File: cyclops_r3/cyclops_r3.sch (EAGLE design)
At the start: 105 parts, among them Q1 BC817, Q2 IRF510, U1 MCP4921, U2 MCP4022-50k, U3 317-N, U4 TLV3701, U5 337-N, U6 ADR03, U7 OP1177, U8 LTC2052HV, U9 ZXTD45

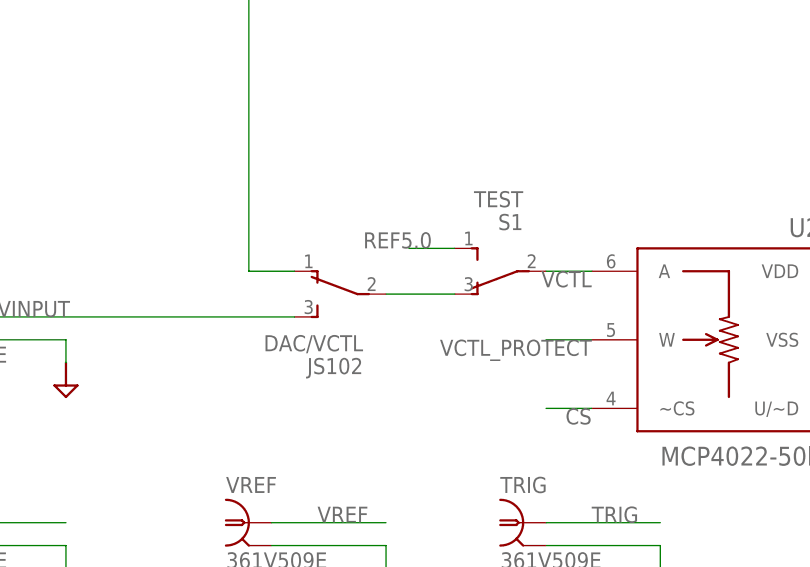
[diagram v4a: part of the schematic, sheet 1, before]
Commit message: The hole size for the solder lugs on the DAC/VCTL switch were too small. This has been fixed.
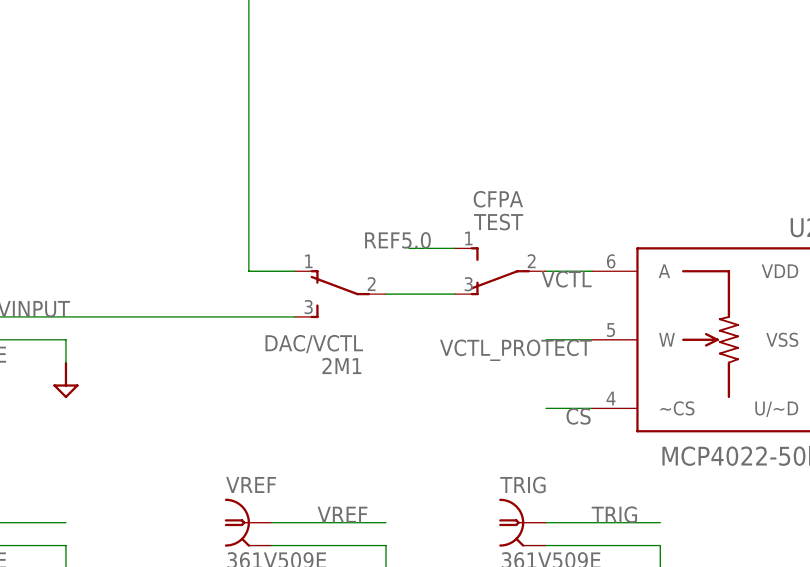
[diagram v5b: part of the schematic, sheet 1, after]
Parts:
- DAC/VCTL: value JS102 -> 2M1
- TEST: value TEST -> CFPA
- renumbered S1 to TEST
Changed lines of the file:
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@@
 <part name="C17" library="cyclops" deviceset="C" device="_0805" value="1uF"/>
 <part name="C11" library="cyclops" deviceset="C-POL" device="_0807" value="100uF"/>
-<part name="S1" library="cyclops" deviceset="SPDT" device="_CFPA" value="TEST"/>
+<part name="TEST" library="cyclops" deviceset="SPDT" device="_CFPA" value="CFPA"/>
 <part name="U9" library="cyclops" deviceset="ZXTD4591E6" device="" value="ZXTD45"/>
 <part name="Q2" library="cyclops" deviceset="N-MOSFET" device="TO-262" value="IRF510"/>
@@
 <part name="PWR_IN" library="cyclops" deviceset="PINH1X3" device="_MINI-JR" value="PINH1X3_MINI-JR"/>
 <part name="GAIN" library="cyclops" deviceset="POT_US" device="_3310" value="1k"/>
-<part name="DAC/VCTL" library="cyclops" deviceset="SPDT" device="_MTS-M6" value="JS102"/>
+<part name="DAC/VCTL" library="cyclops" deviceset="SPDT" device="_MTS-M6" value="2M1"/>
 <part name="L6" library="cyclops" deviceset="L" device="_0603" value="MPZ1608"/>
 <part name="L5" library="cyclops" deviceset="L" device="_0603" value="MPZ1608"/>
@@
 <instance part="FRAME1" gate="G$1" x="-12.7" y="-68.58"/>
 <instance part="FRAME1" gate="G$2" x="160.02" y="-68.58"/>
-<instance part="S1" gate="G$1" x="210.82" y="20.32" rot="R180"/>
+<instance part="TEST" gate="G$1" x="210.82" y="20.32" rot="R180"/>
 <instance part="VAUX_OUT" gate="G$1" x="109.22" y="15.24"/>
 <instance part="CS1" gate="1" x="109.22" y="121.92" smashed="yes">
@@
 <segment>
 <wire x1="195.58" y1="17.78" x2="203.2" y2="17.78" width="0.1524" layer="91"/>
-<pinref part="S1" gate="G$1" pin="1"/>
+<pinref part="TEST" gate="G$1" pin="1"/>
 <pinref part="DAC/VCTL" gate="G$1" pin="2"/>
 </segment>
@@
 <net name="VCTL" class="0">
 <segment>
-<pinref part="S1" gate="G$1" pin="2"/>
+<pinref part="TEST" gate="G$1" pin="2"/>
 <wire x1="213.36" y1="20.32" x2="218.44" y2="20.32" width="0.1524" layer="91"/>
 <pinref part="U2" gate="G$1" pin="A"/>
@@
 <net name="REF5.0" class="0">
 <segment>
-<pinref part="S1" gate="G$1" pin="3"/>
+<pinref part="TEST" gate="G$1" pin="3"/>
 <wire x1="203.2" y1="22.86" x2="198.12" y2="22.86" width="0.1524" layer="91"/>
 <label x="193.04" y="22.86" size="1.778" layer="95"/>

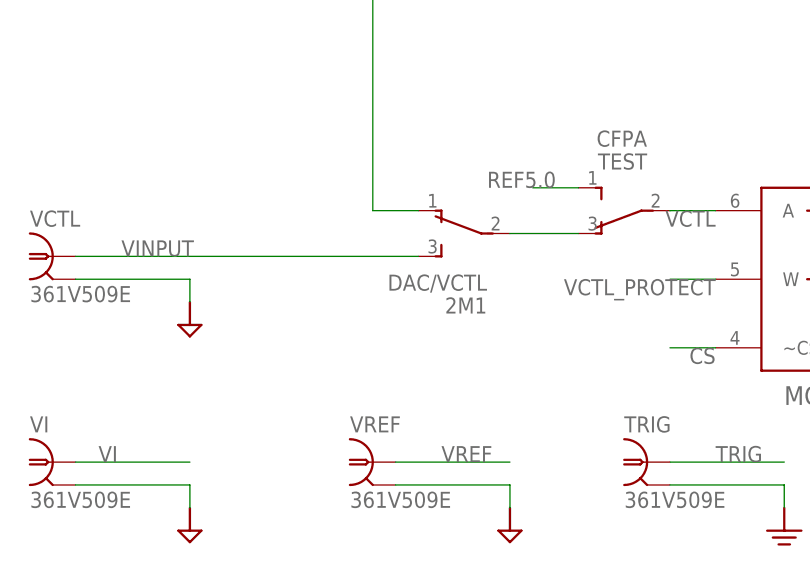
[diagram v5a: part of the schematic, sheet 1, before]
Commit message: Assembed r3.3 and started a TODO list. Started driver code.
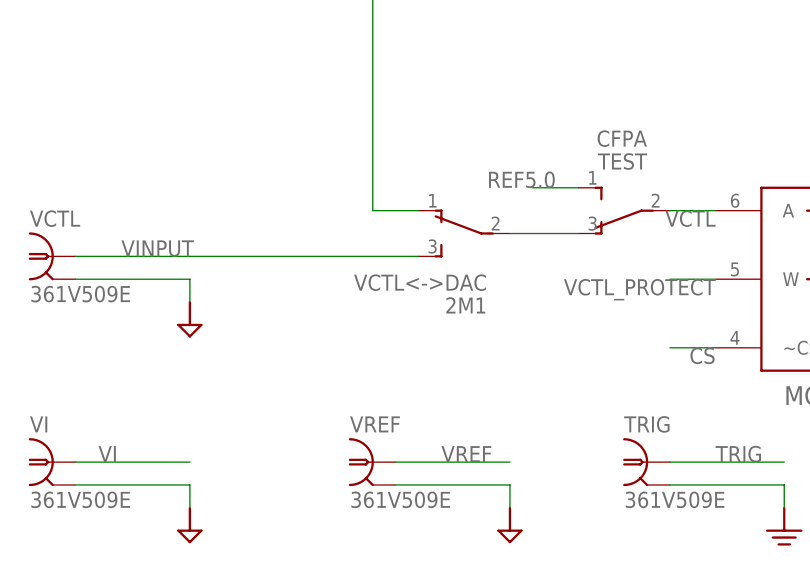
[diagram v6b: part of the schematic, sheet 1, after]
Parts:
- renumbered CURR/AUX to AUX<->CURR, DAC/VCTL to VCTL<->DAC
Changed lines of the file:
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@@
 <?xml version="1.0" encoding="utf-8"?>
 <!DOCTYPE eagle SYSTEM "eagle.dtd">
-<eagle version="6.5.0">
+<eagle version="6.6.0">
 <drawing>
 <settings>
@@
 <part name="D3" library="cyclops" deviceset="S-DIODE" device="SOD-123" value="DS11015"/>
 <part name="D2" library="cyclops" deviceset="S-DIODE" device="SOD-123" value="DS11015"/>
-<part name="CURR/AUX" library="cyclops" deviceset="SPDT" device="_JS" value="JS102"/>
+<part name="AUX&lt;-&gt;CURR" library="cyclops" deviceset="SPDT" device="_JS" value="JS102"/>
 <part name="FRAME1" library="cyclops" deviceset="FRAME_A_L" device=""/>
 <part name="FRAME2" library="cyclops" deviceset="FRAME_A_L" device=""/>
@@
 <part name="PWR_IN" library="cyclops" deviceset="PINH1X3" device="_MINI-JR" value="PINH1X3_MINI-JR"/>
 <part name="GAIN" library="cyclops" deviceset="POT_US" device="_3310" value="1k"/>
-<part name="DAC/VCTL" library="cyclops" deviceset="SPDT" device="_MTS-M6" value="2M1"/>
+<part name="VCTL&lt;-&gt;DAC" library="cyclops" deviceset="SPDT" device="_MTS-M6" value="2M1"/>
 <part name="L6" library="cyclops" deviceset="L" device="_0603" value="MPZ1608"/>
 <part name="L5" library="cyclops" deviceset="L" device="_0603" value="MPZ1608"/>
@@
 <instance part="PWR_DIST" gate="G$1" x="33.02" y="-20.32"/>
 <instance part="PWR_IN" gate="G$1" x="25.4" y="5.08"/>
-<instance part="DAC/VCTL" gate="G$1" x="193.04" y="17.78" rot="MR0"/>
+<instance part="VCTL&lt;-&gt;DAC" gate="G$1" x="193.04" y="17.78" rot="MR0"/>
 <instance part="L6" gate="L" x="53.34" y="38.1" smashed="yes">
 <attribute name="NAME" x="52.07" y="30.48" size="1.778" layer="95" rot="R90"/>
@@
 <wire x1="172.72" y1="78.74" x2="172.72" y2="81.28" width="0.1524" layer="91"/>
 <junction x="172.72" y="81.28"/>
-<pinref part="DAC/VCTL" gate="G$1" pin="1"/>
+<pinref part="VCTL&lt;-&gt;DAC" gate="G$1" pin="1"/>
 <wire x1="180.34" y1="20.32" x2="185.42" y2="20.32" width="0.1524" layer="91"/>
 <wire x1="180.34" y1="81.28" x2="180.34" y2="20.32" width="0.1524" layer="91"/>
@@
 <pinref part="VCTL" gate="G$1" pin="1"/>
 <label x="152.4" y="15.24" size="1.778" layer="95"/>
-<pinref part="DAC/VCTL" gate="G$1" pin="3"/>
+<pinref part="VCTL&lt;-&gt;DAC" gate="G$1" pin="3"/>
 <wire x1="185.42" y1="15.24" x2="147.32" y2="15.24" width="0.1524" layer="91"/>
 </segment>
@@
 <wire x1="195.58" y1="17.78" x2="203.2" y2="17.78" width="0.1524" layer="91"/>
 <pinref part="TEST" gate="G$1" pin="1"/>
-<pinref part="DAC/VCTL" gate="G$1" pin="2"/>
+<pinref part="VCTL&lt;-&gt;DAC" gate="G$1" pin="2"/>
 </segment>
 </net>
@@
 <instance part="D3" gate="G$1" x="-10.16" y="73.66" rot="R90"/>
 <instance part="D2" gate="G$1" x="-10.16" y="99.06" rot="R90"/>
-<instance part="CURR/AUX" gate="G$1" x="7.62" y="48.26" rot="MR270"/>
+<instance part="AUX&lt;-&gt;CURR" gate="G$1" x="7.62" y="48.26" rot="MR270"/>
 <instance part="FRAME4" gate="G$1" x="-91.44" y="-58.42"/>
 <instance part="U9" gate="G$1" x="83.82" y="83.82"/>
@@
 <wire x1="10.16" y1="20.32" x2="68.58" y2="20.32" width="0.1524" layer="91"/>
 <junction x="68.58" y="20.32"/>
-<pinref part="CURR/AUX" gate="G$1" pin="3"/>
+<pinref part="AUX&lt;-&gt;CURR" gate="G$1" pin="3"/>
 <wire x1="10.16" y1="40.64" x2="10.16" y2="20.32" width="0.1524" layer="91"/>
 </segment>
@@
 <wire x1="7.62" y1="50.8" x2="7.62" y2="81.28" width="0.1524" layer="91"/>
 <pinref part="U8" gate="B" pin="-IN"/>
-<pinref part="CURR/AUX" gate="G$1" pin="2"/>
+<pinref part="AUX&lt;-&gt;CURR" gate="G$1" pin="2"/>
 </segment>
 </net>
@@
 <wire x1="-35.56" y1="35.56" x2="-35.56" y2="38.1" width="0.1524" layer="91"/>
 <junction x="-35.56" y="35.56"/>
-<pinref part="CURR/AUX" gate="G$1" pin="1"/>
+<pinref part="AUX&lt;-&gt;CURR" gate="G$1" pin="1"/>
 <wire x1="5.08" y1="35.56" x2="5.08" y2="40.64" width="0.1524" layer="91"/>
 <junction x="5.08" y="35.56"/>

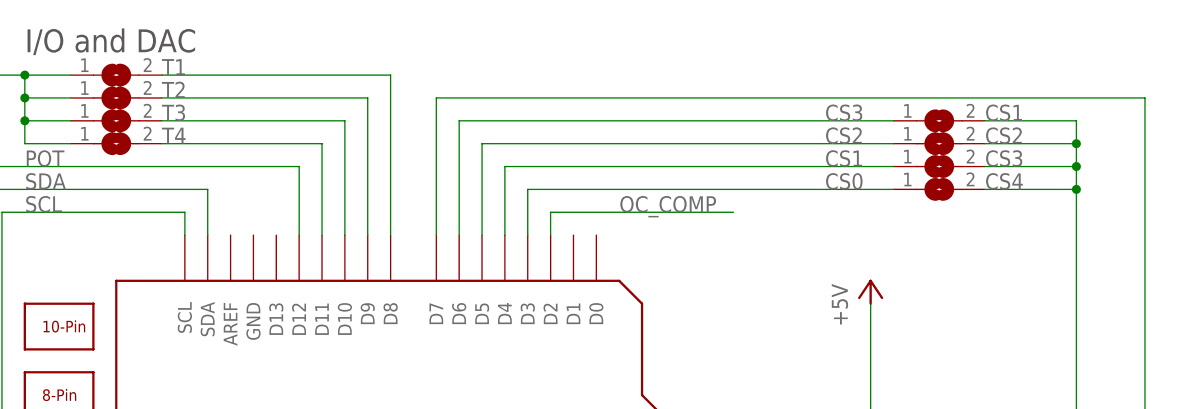
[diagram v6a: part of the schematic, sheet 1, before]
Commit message: Asthetic fixes to board. Driver has limited functionality and is pretty inefficient, but the base stuff is there.
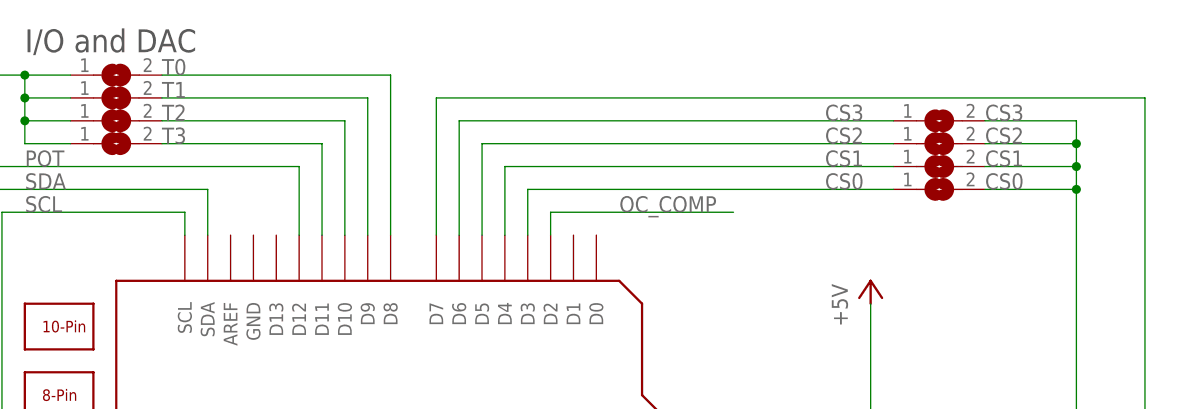
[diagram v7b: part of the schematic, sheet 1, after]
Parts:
- removed T4: (no value), cyclops:SJ
- added T0: (no value), cyclops:SJ
- renumbered CS4 to CS0
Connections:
- net CS1: now also CS1.1; no longer CS3.1
- net CS3: now also CS3.1; no longer CS1.1
- net T0: now also T0.2; no longer T1.2
- net T1: now also T1.2; no longer T2.2
- net T2: now also T2.2; no longer T3.2
- net T3: now also T3.2; no longer T4.2
- net TRIG: now also T0.1; no longer T4.1
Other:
- moved on the sheet: CS1, CS3, T1, T2, T3
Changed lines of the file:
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@@
 <part name="C24" library="cyclops" deviceset="C" device="_0805" value="1uF"/>
 <part name="C22" library="cyclops" deviceset="C" device="_0603" value=".1uF"/>
+<part name="CS3" library="cyclops" deviceset="SJ" device=""/>
+<part name="CS2" library="cyclops" deviceset="SJ" device=""/>
 <part name="CS1" library="cyclops" deviceset="SJ" device=""/>
-<part name="CS2" library="cyclops" deviceset="SJ" device=""/>
-<part name="CS3" library="cyclops" deviceset="SJ" device=""/>
-<part name="CS4" library="cyclops" deviceset="SJ" device=""/>
+<part name="CS0" library="cyclops" deviceset="SJ" device=""/>
 <part name="Q1" library="cyclops" deviceset="BC817*" device="SMD" technology="-16" value="BC817"/>
 <part name="R8" library="cyclops" deviceset="R" device="_0603" value="10k"/>
@@
 <part name="P+5" library="cyclops" deviceset="+5V" device="" value="+12V"/>
 <part name="R20" library="cyclops" deviceset="R" device="_0603" value="220k"/>
+<part name="T0" library="cyclops" deviceset="SJ" device=""/>
 <part name="T1" library="cyclops" deviceset="SJ" device=""/>
 <part name="T2" library="cyclops" deviceset="SJ" device=""/>
 <part name="T3" library="cyclops" deviceset="SJ" device=""/>
-<part name="T4" library="cyclops" deviceset="SJ" device=""/>
 <part name="TRIG" library="cyclops" deviceset="BNC" device="_V-BITE" value="361V509E"/>
 <part name="U$47" library="cyclops" deviceset="GND1" device=""/>
@@
 <instance part="TEST" gate="G$1" x="210.82" y="20.32" rot="R180"/>
 <instance part="VAUX_OUT" gate="G$1" x="109.22" y="15.24"/>
-<instance part="CS1" gate="1" x="109.22" y="121.92" smashed="yes">
+<instance part="CS3" gate="1" x="109.22" y="121.92" smashed="yes">
 <attribute name="NAME" x="114.3" y="121.92" size="1.778" layer="95"/>
 <attribute name="VALUE" x="106.68" y="118.11" size="1.778" layer="96"/>
@@
 <attribute name="VALUE" x="106.68" y="115.57" size="1.778" layer="96"/>
 </instance>
-<instance part="CS3" gate="1" x="109.22" y="116.84" smashed="yes">
+<instance part="CS1" gate="1" x="109.22" y="116.84" smashed="yes">
 <attribute name="NAME" x="114.3" y="116.84" size="1.778" layer="95"/>
 <attribute name="VALUE" x="106.68" y="113.03" size="1.778" layer="96"/>
 </instance>
-<instance part="CS4" gate="1" x="109.22" y="114.3" smashed="yes">
+<instance part="CS0" gate="1" x="109.22" y="114.3" smashed="yes">
 <attribute name="NAME" x="114.3" y="114.3" size="1.778" layer="95"/>
 <attribute name="VALUE" x="106.68" y="110.49" size="1.778" layer="96"/>
@@
 <instance part="LED-" gate="G$1" x="73.66" y="0" rot="R180"/>
 <instance part="LED+" gate="G$1" x="73.66" y="10.16" rot="R180"/>
-<instance part="T1" gate="1" x="17.78" y="127" smashed="yes">
+<instance part="T0" gate="1" x="17.78" y="127" smashed="yes">
 <attribute name="NAME" x="22.86" y="127" size="1.778" layer="95"/>
 <attribute name="VALUE" x="15.24" y="123.19" size="1.778" layer="96"/>
 </instance>
-<instance part="T2" gate="1" x="17.78" y="124.46" smashed="yes">
+<instance part="T1" gate="1" x="17.78" y="124.46" smashed="yes">
 <attribute name="NAME" x="22.86" y="124.46" size="1.778" layer="95"/>
 <attribute name="VALUE" x="15.24" y="120.65" size="1.778" layer="96"/>
 </instance>
-<instance part="T3" gate="1" x="17.78" y="121.92" smashed="yes">
+<instance part="T2" gate="1" x="17.78" y="121.92" smashed="yes">
 <attribute name="NAME" x="22.86" y="121.92" size="1.778" layer="95"/>
 <attribute name="VALUE" x="15.24" y="118.11" size="1.778" layer="96"/>
 </instance>
-<instance part="T4" gate="1" x="17.78" y="119.38" smashed="yes">
+<instance part="T3" gate="1" x="17.78" y="119.38" smashed="yes">
 <attribute name="NAME" x="22.86" y="119.38" size="1.778" layer="95"/>
 <attribute name="VALUE" x="15.24" y="115.57" size="1.778" layer="96"/>
@@
 <segment>
 <label x="96.52" y="114.3" size="1.778" layer="95"/>
-<pinref part="CS4" gate="1" pin="1"/>
+<pinref part="CS0" gate="1" pin="1"/>
 <pinref part="LEONARDO" gate="G$1" pin="D3"/>
 <wire x1="63.5" y1="114.3" x2="104.14" y2="114.3" width="0.1524" layer="91"/>
@@
 <segment>
 <label x="96.52" y="116.84" size="1.778" layer="95"/>
-<pinref part="CS3" gate="1" pin="1"/>
+<pinref part="CS1" gate="1" pin="1"/>
 <pinref part="LEONARDO" gate="G$1" pin="D4"/>
 <wire x1="60.96" y1="116.84" x2="104.14" y2="116.84" width="0.1524" layer="91"/>
@@
 <segment>
 <label x="96.52" y="121.92" size="1.778" layer="95"/>
-<pinref part="CS1" gate="1" pin="1"/>
+<pinref part="CS3" gate="1" pin="1"/>
 <pinref part="LEONARDO" gate="G$1" pin="D6"/>
 <wire x1="55.88" y1="121.92" x2="104.14" y2="121.92" width="0.1524" layer="91"/>
@@
 <wire x1="114.3" y1="114.3" x2="124.46" y2="114.3" width="0.1524" layer="91"/>
 <junction x="124.46" y="114.3"/>
-<pinref part="CS4" gate="1" pin="2"/>
+<pinref part="CS0" gate="1" pin="2"/>
+<pinref part="CS1" gate="1" pin="2"/>
+<pinref part="CS2" gate="1" pin="2"/>
 <pinref part="CS3" gate="1" pin="2"/>
-<pinref part="CS2" gate="1" pin="2"/>
-<pinref part="CS1" gate="1" pin="2"/>
 </segment>
 <segment>
@@
 <segment>
 <wire x1="0" y1="127" x2="7.62" y2="127" width="0.1524" layer="91"/>
+<pinref part="T0" gate="1" pin="1"/>
 <pinref part="T1" gate="1" pin="1"/>
-<pinref part="T2" gate="1" pin="1"/>
 <wire x1="7.62" y1="127" x2="12.7" y2="127" width="0.1524" layer="91"/>
 <wire x1="12.7" y1="124.46" x2="7.62" y2="124.46" width="0.1524" layer="91"/>
 <wire x1="7.62" y1="124.46" x2="7.62" y2="127" width="0.1524" layer="91"/>
 <junction x="7.62" y="127"/>
-<pinref part="T3" gate="1" pin="1"/>
+<pinref part="T2" gate="1" pin="1"/>
 <wire x1="12.7" y1="121.92" x2="7.62" y2="121.92" width="0.1524" layer="91"/>
 <wire x1="7.62" y1="121.92" x2="7.62" y2="124.46" width="0.1524" layer="91"/>
 <junction x="7.62" y="124.46"/>
-<pinref part="T4" gate="1" pin="1"/>
+<pinref part="T3" gate="1" pin="1"/>
 <wire x1="12.7" y1="119.38" x2="7.62" y2="119.38" width="0.1524" layer="91"/>
 <wire x1="7.62" y1="119.38" x2="7.62" y2="121.92" width="0.1524" layer="91"/>
@@
 <net name="T0" class="0">
 <segment>
-<pinref part="T1" gate="1" pin="2"/>
+<pinref part="T0" gate="1" pin="2"/>
 <wire x1="22.86" y1="127" x2="48.26" y2="127" width="0.1524" layer="91"/>
 <pinref part="LEONARDO" gate="G$1" pin="D8"/>
@@
 <net name="T1" class="0">
 <segment>
-<pinref part="T2" gate="1" pin="2"/>
+<pinref part="T1" gate="1" pin="2"/>
 <wire x1="22.86" y1="124.46" x2="45.72" y2="124.46" width="0.1524" layer="91"/>
 <pinref part="LEONARDO" gate="G$1" pin="D9"/>
@@
 <net name="T2" class="0">
 <segment>
-<pinref part="T3" gate="1" pin="2"/>
+<pinref part="T2" gate="1" pin="2"/>
 <wire x1="22.86" y1="121.92" x2="43.18" y2="121.92" width="0.1524" layer="91"/>
 <pinref part="LEONARDO" gate="G$1" pin="D10"/>
@@
 <net name="T3" class="0">
 <segment>
-<pinref part="T4" gate="1" pin="2"/>
+<pinref part="T3" gate="1" pin="2"/>
 <wire x1="22.86" y1="119.38" x2="40.64" y2="119.38" width="0.1524" layer="91"/>
 <pinref part="LEONARDO" gate="G$1" pin="D11"/>
